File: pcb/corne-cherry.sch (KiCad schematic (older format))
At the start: 146 parts, among them J1 MJ-4PP-9, J2 OLED, J3 MJ-4PP-9, J4 OLED, J5 Conn_01x01_Male, J6 Conn_01x01_Male, P1 Conn_01x03, P3 Conn_01x03, SW1 SW_PUSH, SW10 SW_PUSH, SW11 SW_PUSH, SW12 SW_PUSH, SW13 SW_PUSH, SW14 SW_PUSH, SW15 SW_PUSH, SW16 SW_PUSH, SW17 SW_PUSH, SW18 SW_PUSH, SW19 SW_PUSH, SW2 SW_PUSH, SW20 SW_PUSH, SW21 SW_PUSH, SW22 SW_PUSH, SW23 SW_PUSH, SW24 SW_PUSH, SW25 SW_PUSH, SW26 SW_PUSH, SW27 SW_PUSH, SW28 SW_PUSH, SW29 SW_PUSH, SW3 SW_PUSH, SW30 SW_PUSH, SW31 SW_PUSH, SW32 SW_PUSH, SW33 SW_PUSH, SW34 SW_PUSH, SW35 SW_PUSH, SW36 SW_PUSH, SW37 SW_PUSH, SW38 SW_PUSH, SW39 SW_PUSH, SW4 SW_PUSH, SW40 SW_PUSH, SW41 SW_PUSH, SW42 SW_PUSH, SW43 Rotary_Encoder_Switch, SW44 Rotary_Encoder_Switch, SW5 SW_PUSH, SW6 SW_PUSH, SW7 SW_PUSH, SW8 SW_PUSH, SW9 SW_PUSH, U1 ProMicro, U2 ProMicro

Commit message: Add trackball support
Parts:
- added J7: Conn_01x05, other_parts:pimoroni_left_side_mount, symbol Connector_Generic:Conn_01x05
- J1, J3: symbol kbd:MJ-4PP-9 -> corne-cherry-rescue:MJ-4PP-9-kbd
- LED1, LED10, LED11, LED12, LED13, LED14, LED15, LED16, LED17, LED18, LED19, LED2, LED20, LED21, LED22, LED23, LED24, LED25, LED26, LED27, LED28, LED29, LED3, LED30, LED31, LED32, LED33, LED34, LED35, LED36, LED37, LED38, LED39, LED4, LED40, LED41, LED42, LED5, LED6, LED7, LED8, LED9: symbol kbd:YS-SK6812MINI-E -> corne-cherry-rescue:YS-SK6812MINI-E-kbd
- RSW1, RSW2, SW1, SW10, SW11, SW12, SW13, SW14, SW15, SW16, SW17, SW18, SW19, SW2, SW20, SW21, SW22, SW23, SW24, SW25, SW26, SW27, SW28, SW29, SW3, SW30, SW31, SW32, SW33, SW34, SW35, SW36, SW37, SW38, SW39, SW4, SW40, SW41, SW42, SW5, SW6, SW7, SW8, SW9: symbol kbd:SW_PUSH -> corne-cherry-rescue:SW_PUSH-kbd
- U1, U2: symbol kbd:ProMicro -> corne-cherry-rescue:ProMicro-kbd
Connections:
- wire segments 309 -> 313
- no-connect marks 8 -> 9

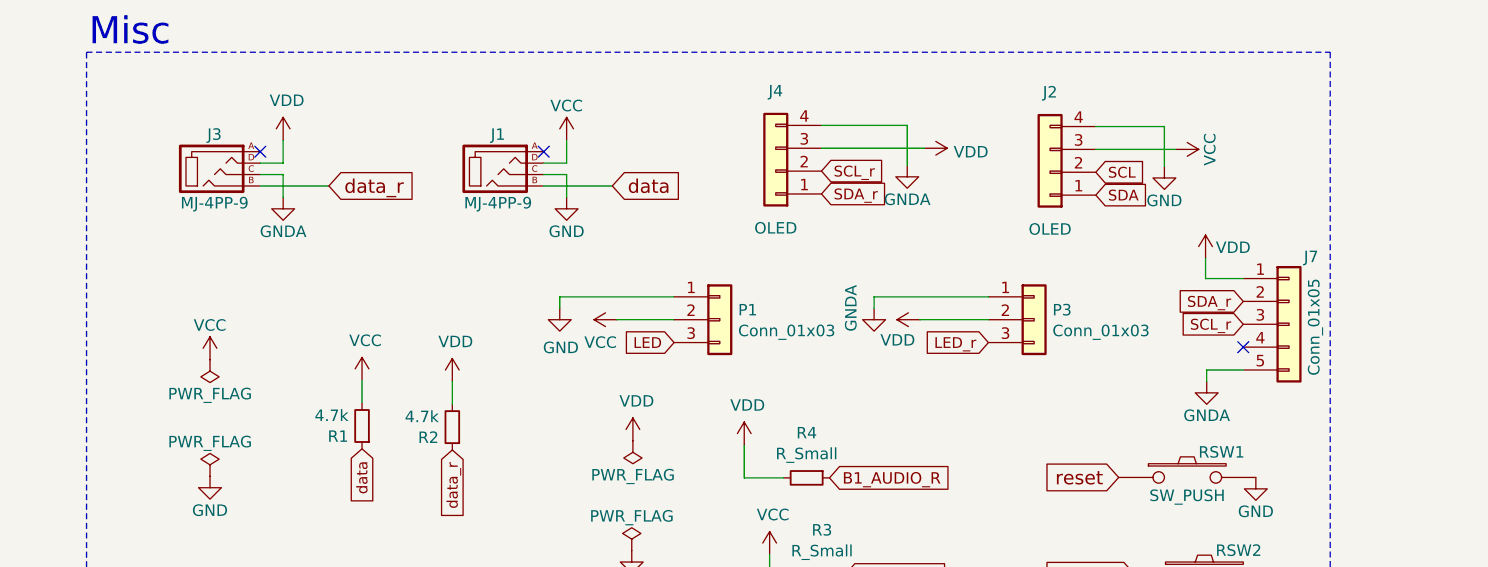
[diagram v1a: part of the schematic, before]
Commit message: Update markers and silkscreen
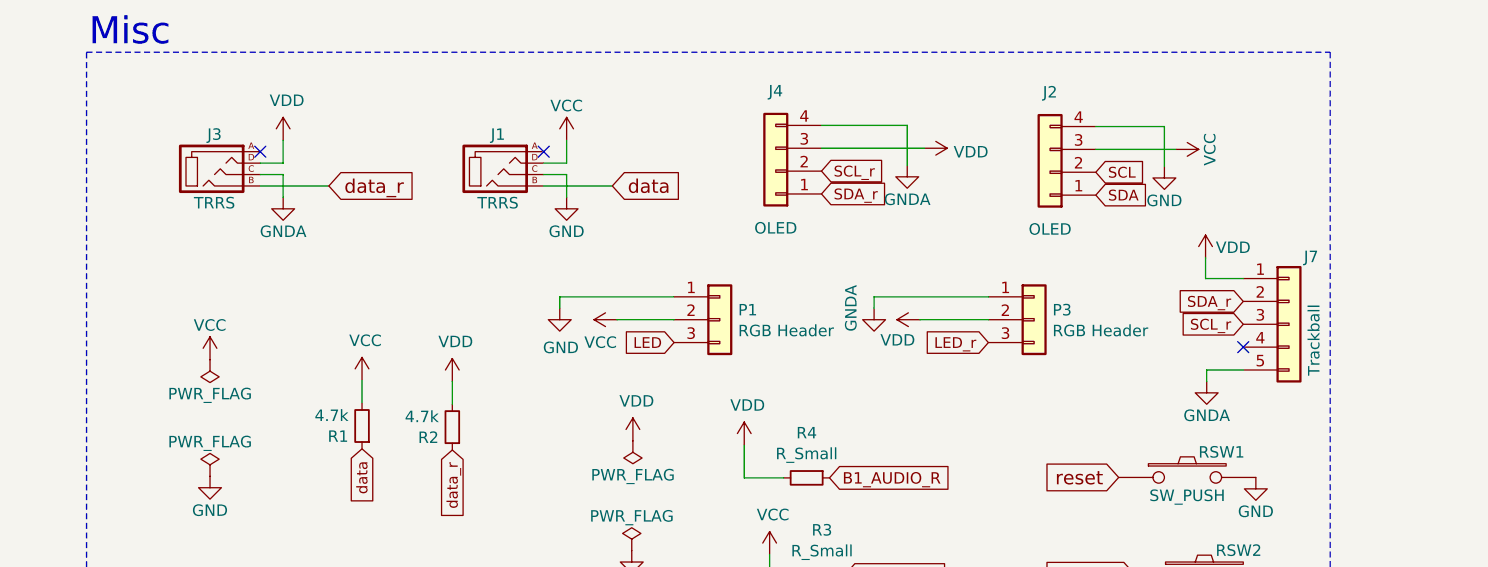
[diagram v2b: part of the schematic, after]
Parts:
- J1, J3: value MJ-4PP-9 -> TRRS
- J7: value Conn_01x05 -> Trackball
- P1, P3: value Conn_01x03 -> RGB Header
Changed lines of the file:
@@
 P 3910 1325
 F 0 "J1" H 3910 1475 50  0000 C CNN
-F 1 "MJ-4PP-9" H 3910 1175 50  0000 C CNN
+F 1 "TRRS" H 3910 1175 50  0000 C CNN
 F 2 "kbd:MJ-4PP-9_1side" H 4185 1500 50  0001 C CNN
 F 3 "" H 4185 1500 50  0001 C CNN
@@
 P 2670 1325
 F 0 "J3" H 2670 1475 50  0000 C CNN
-F 1 "MJ-4PP-9" H 2670 1175 50  0000 C CNN
+F 1 "TRRS" H 2670 1175 50  0000 C CNN
 F 2 "kbd:MJ-4PP-9_1side" H 2945 1500 50  0001 C CNN
 F 3 "" H 2945 1500 50  0001 C CNN
@@
 P 6255 1985
 F 0 "P3" H 6335 2027 50  0000 L CNN
-F 1 "Conn_01x03" H 6335 1936 50  0000 L CNN
+F 1 "RGB Header" H 6335 1936 50  0000 L CNN
 F 2 "Connector_PinSocket_2.54mm:PinSocket_1x03_P2.54mm_Horizontal" H 6255 1985 50  0001 C CNN
 F 3 "~" H 6255 1985 50  0001 C CNN
@@
 P 4880 1985
 F 0 "P1" H 4960 2027 50  0000 L CNN
-F 1 "Conn_01x03" H 4960 1936 50  0000 L CNN
+F 1 "RGB Header" H 4960 1936 50  0000 L CNN
 F 2 "Connector_PinSocket_2.54mm:PinSocket_1x03_P2.54mm_Vertical" H 4880 1985 50  0001 C CNN
 F 3 "~" H 4880 1985 50  0001 C CNN
@@
 P 7370 2005
 F 0 "J7" H 7435 2300 50  0000 L CNN
-F 1 "Conn_01x05" V 7480 1780 50  0000 L CNN
+F 1 "Trackball" V 7480 1780 50  0000 L CNN
 F 2 "other_parts:pimoroni_left_side_mount" H 7370 2005 50  0001 C CNN
 F 3 "~" H 7370 2005 50  0001 C CNN

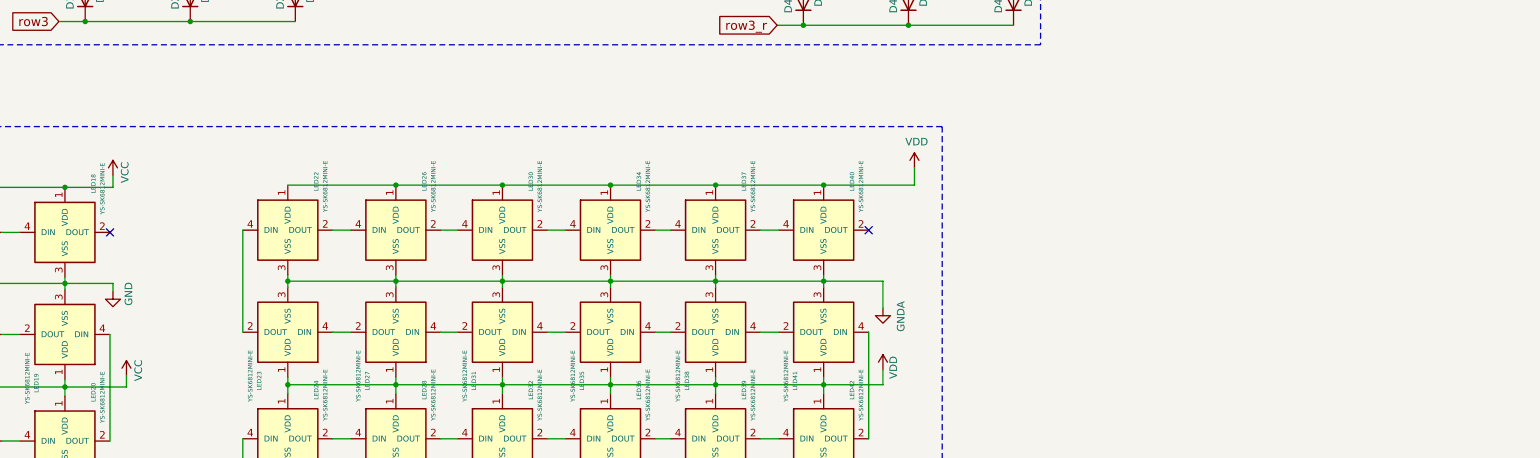
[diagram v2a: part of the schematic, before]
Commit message: some underglow stuff on left half
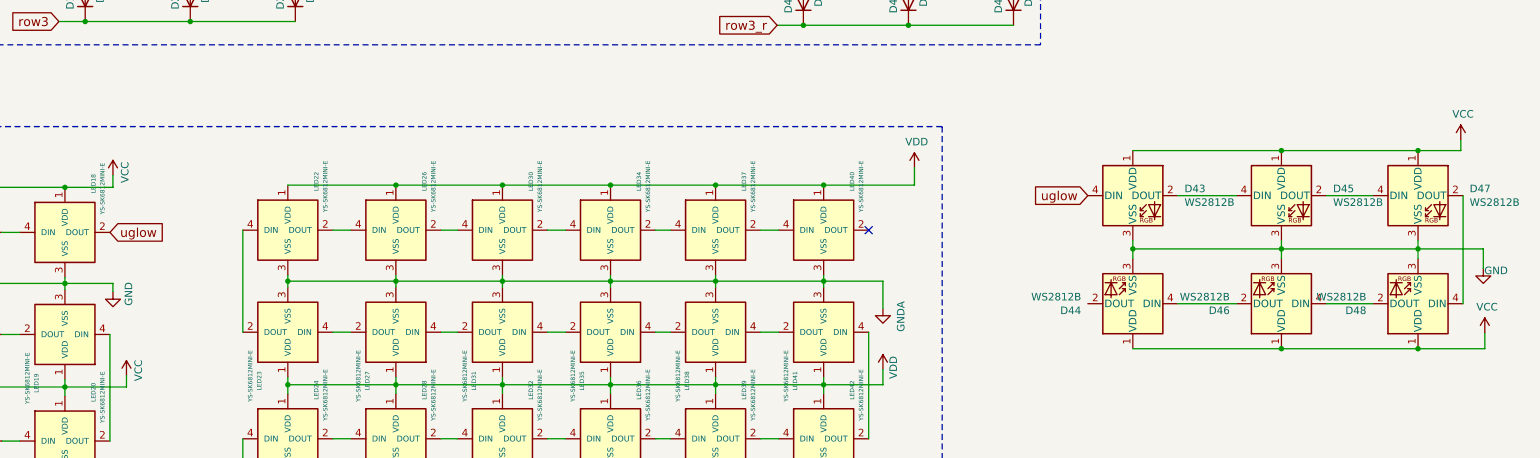
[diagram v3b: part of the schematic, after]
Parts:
- added D43, D44, D45, D46, D47, D48: WS2812B, Keebio-Parts:WS2812B, symbol LED:WS2812B
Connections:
- net GND: now also D43.3 (VSS), D44.3 (VSS), D45.3 (VSS), D46.3 (VSS), D47.3 (VSS), D48.3 (VSS)
- net VCC: now also D43.1 (VDD), D44.1 (VDD), D45.1 (VDD), D46.1 (VDD), D47.1 (VDD), D48.1 (VDD)
- net uglow: now reaches LED18.2 (DOUT)
- net uglow: now also D43.4 (DIN)
- new net: D43.2 (DOUT), D45.4 (DIN)
- new net: D45.2 (DOUT), D47.4 (DIN)
- new net: D47.2 (DOUT), D48.4 (DIN)
- new net: D46.4 (DIN), D48.2 (DOUT)
- new net: D44.4 (DIN), D46.2 (DOUT)
- no-connect marks 9 -> 8
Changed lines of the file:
@@
 Wire Wire Line
 	1420 8990 1300 8990
-NoConn ~ 4870 8310
 Wire Wire Line
 	1000 8650 1720 8650
@@
 Text GLabel 7170 2005 0    47   Input ~ 0
 SCL_r
+$Comp
+L LED:WS2812B D43
+U 1 1 60D8D511
+P 11685 8065
+F 0 "D43" H 12029 8111 50  0000 L CNN
+F 1 "WS2812B" H 12029 8020 50  0000 L CNN
+F 2 "Keebio-Parts:WS2812B" H 11735 7765 50  0001 L TNN
+F 3 "https://cdn-shop.adafruit.com/datasheets/WS2812B.pdf" H 11785 7690 50  0001 L TNN
+	1    11685 8065
+	1    0    0    -1
+$EndComp
+$Comp
+L LED:WS2812B D45
+U 1 1 60D8F5FE
+P 12675 8065
+F 0 "D45" H 13019 8111 50  0000 L CNN
+F 1 "WS2812B" H 13019 8020 50  0000 L CNN
+F 2 "Keebio-Parts:WS2812B" H 12725 7765 50  0001 L TNN
+F 3 "https://cdn-shop.adafruit.com/datasheets/WS2812B.pdf" H 12775 7690 50  0001 L TNN
+	1    12675 8065
+	1    0    0    -1
+$EndComp
+Wire Wire Line
+	11985 8065 12375 8065
+$Comp
+L LED:WS2812B D47
+U 1 1 60DAA5B2
+P 13585 8065
+F 0 "D47" H 13929 8111 50  0000 L CNN
+F 1 "WS2812B" H 13929 8020 50  0000 L CNN
+F 2 "Keebio-Parts:WS2812B" H 13635 7765 50  0001 L TNN
+F 3 "https://cdn-shop.adafruit.com/datasheets/WS2812B.pdf" H 13685 7690 50  0001 L TNN
+	1    13585 8065
+	1    0    0    -1
+$EndComp
+Wire Wire Line
+	12975 8065 13285 8065
+$Comp
+L LED:WS2812B D48
+U 1 1 60DC8763
+P 13585 8785
+F 0 "D48" H 13929 8831 50  0000 L CNN
+F 1 "WS2812B" H 13929 8740 50  0000 L CNN
+F 2 "Keebio-Parts:WS2812B" H 13635 8485 50  0001 L TNN
+F 3 "https://cdn-shop.adafruit.com/datasheets/WS2812B.pdf" H 13685 8410 50  0001 L TNN
+	1    13585 8785
+	-1   0    0    1
+$EndComp
+$Comp
+L LED:WS2812B D46
+U 1 1 60DC8CAF
+P 12675 8785
+F 0 "D46" H 13019 8831 50  0000 L CNN
+F 1 "WS2812B" H 13019 8740 50  0000 L CNN
+F 2 "Keebio-Parts:WS2812B" H 12725 8485 50  0001 L TNN
+F 3 "https://cdn-shop.adafruit.com/datasheets/WS2812B.pdf" H 12775 8410 50  0001 L TNN
+	1    12675 8785
+	-1   0    0    1
+$EndComp
+Wire Wire Line
+	11985 8785 12375 8785
+$Comp
+L LED:WS2812B D44
+U 1 1 60DC8CBA
+P 11685 8785
+F 0 "D44" H 12029 8831 50  0000 L CNN
+F 1 "WS2812B" H 12029 8740 50  0000 L CNN
+F 2 "Keebio-Parts:WS2812B" H 11735 8485 50  0001 L TNN
+F 3 "https://cdn-shop.adafruit.com/datasheets/WS2812B.pdf" H 11785 8410 50  0001 L TNN
+	1    11685 8785
+	-1   0    0    1
+$EndComp
+Wire Wire Line
+	12975 8785 13285 8785
+Text GLabel 4870 8310 2    60   Input ~ 0
+uglow
+Text GLabel 11385 8065 0    60   Input ~ 0
+uglow
+Wire Wire Line
+	13885 8065 13885 8785
+Wire Wire Line
+	11685 8485 11685 8420
+Wire Wire Line
+	11685 8420 12675 8420
+Wire Wire Line
+	14020 8420 14020 8550
+Wire Wire Line
+	11685 8365 11685 8420
+Connection ~ 11685 8420
+Wire Wire Line
+	12675 8485 12675 8420
+Connection ~ 12675 8420
+Wire Wire Line
+	12675 8420 13585 8420
+Wire Wire Line
+	12675 8365 12675 8420
+Wire Wire Line
+	13585 8485 13585 8420
+Connection ~ 13585 8420
+Wire Wire Line
+	13585 8420 14020 8420
+Wire Wire Line
+	13585 8365 13585 8420
+$Comp
+L power:GND #PWR0123
+U 1 1 60F413B7
+P 14020 8550
+F 0 "#PWR0123" H 14020 8300 50  0001 C CNN
+F 1 "GND" H 14105 8535 50  0000 C CNN
+F 2 "" H 14020 8550 50  0001 C CNN
+F 3 "" H 14020 8550 50  0001 C CNN
+	1    14020 8550
+	1    0    0    -1
+$EndComp
+Wire Wire Line
+	11685 7765 12675 7765
+Wire Wire Line
+	13870 7765 13870 7695
+Connection ~ 12675 7765
+Wire Wire Line
+	12675 7765 13585 7765
+Connection ~ 13585 7765
+Wire Wire Line
+	13585 7765 13870 7765
+$Comp
+L power:VCC #PWR0124
+U 1 1 60FEAFF3
+P 13870 7695
+F 0 "#PWR0124" H 13870 7545 50  0001 C CNN
+F 1 "VCC" H 13885 7868 50  0000 C CNN
+F 2 "" H 13870 7695 50  0001 C CNN
+F 3 "" H 13870 7695 50  0001 C CNN
+	1    13870 7695
+	1    0    0    -1
+$EndComp
+Wire Wire Line
+	11685 9085 12675 9085
+Wire Wire Line
+	14030 9085 14030 8980
+Connection ~ 12675 9085
+Wire Wire Line
+	12675 9085 13585 9085
+Connection ~ 13585 9085
+Wire Wire Line
+	13585 9085 14030 9085
+$Comp
+L power:VCC #PWR0125
+U 1 1 6100B6CC
+P 14030 8980
+F 0 "#PWR0125" H 14030 8830 50  0001 C CNN
+F 1 "VCC" H 14045 9153 50  0000 C CNN
+F 2 "" H 14030 8980 50  0001 C CNN
+F 3 "" H 14030 8980 50  0001 C CNN
+	1    14030 8980
+	1    0    0    -1
+$EndComp
 $EndSCHEMATC

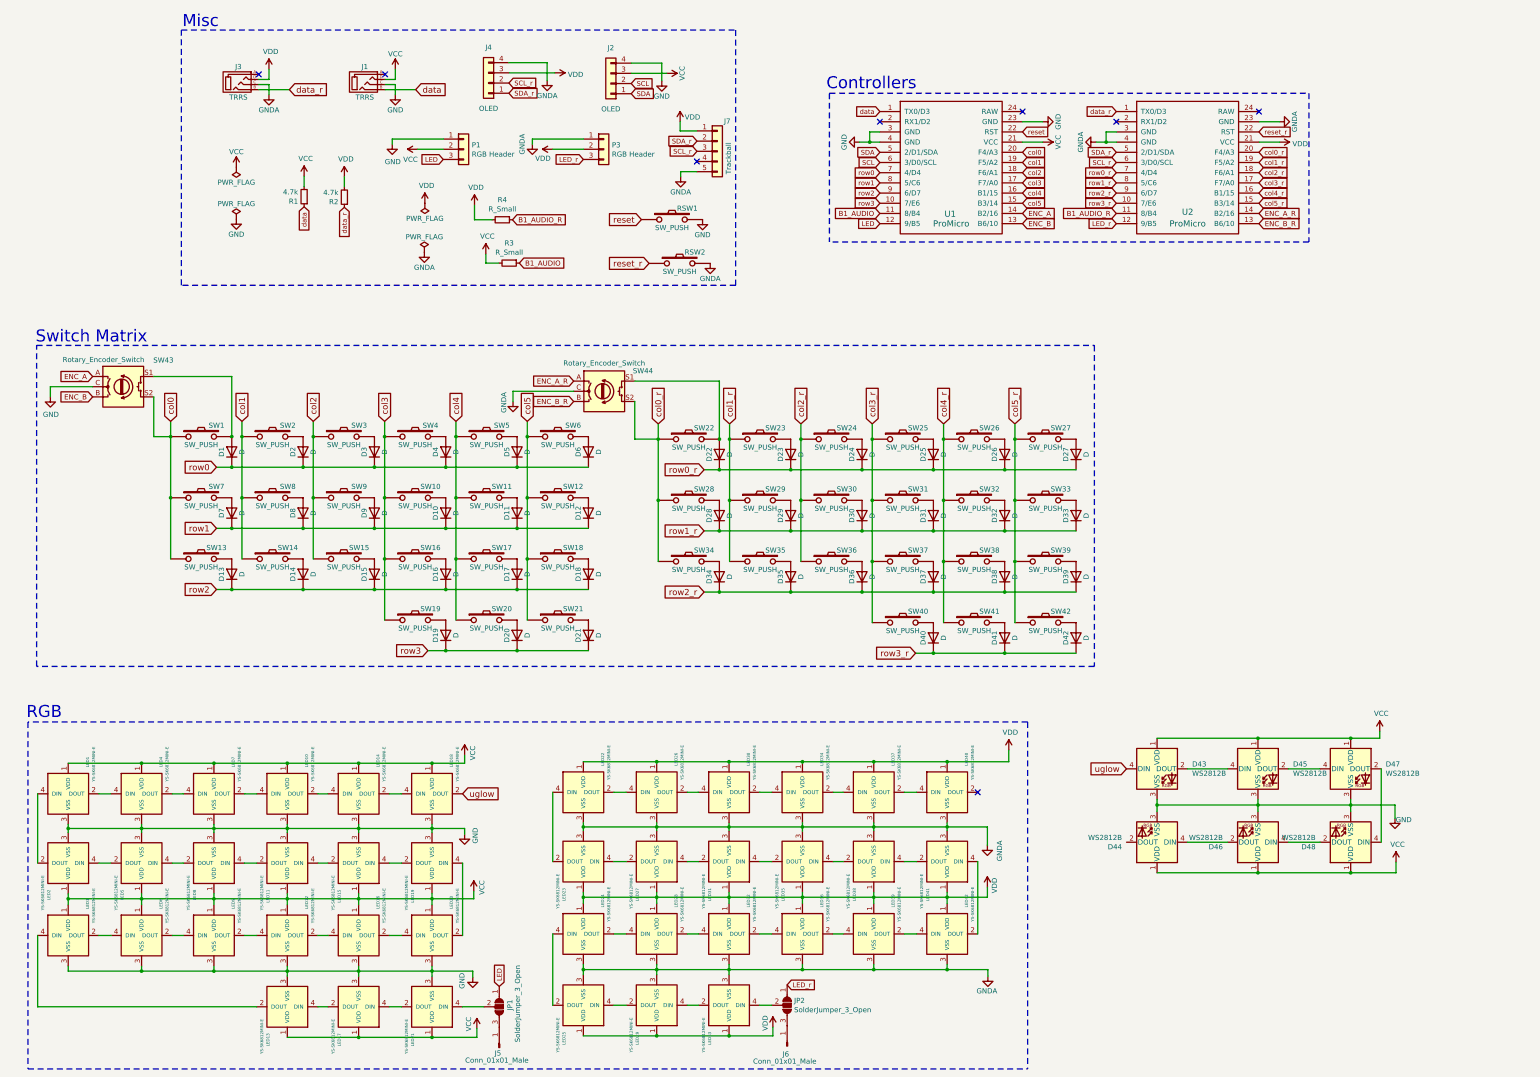
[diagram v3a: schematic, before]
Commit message: Finish underglow and add SMD resistor foorprints
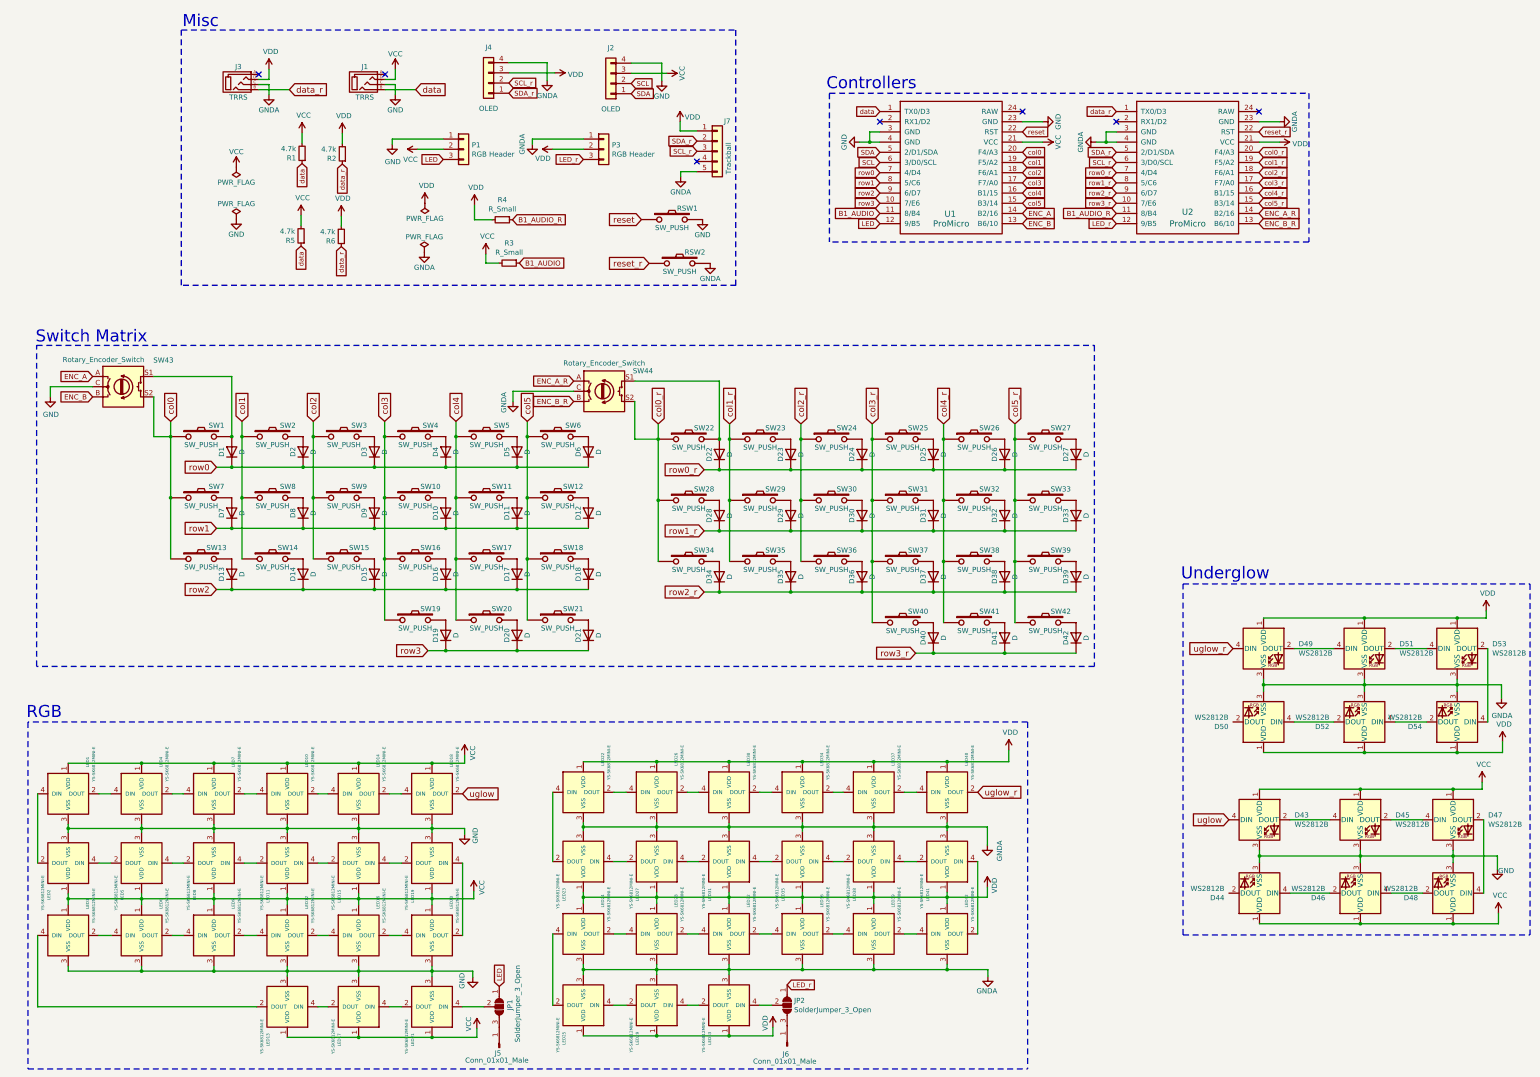
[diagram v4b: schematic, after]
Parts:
- added D49, D50, D51, D52, D53, D54: WS2812B, Keebio-Parts:WS2812B, symbol LED:WS2812B
- added R5, R6: 4.7k, Keebio-Parts:R_0805, symbol Device:R_Small
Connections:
- net GNDA: now also D49.3 (VSS), D50.3 (VSS), D51.3 (VSS), D52.3 (VSS), D53.3 (VSS), D54.3 (VSS)
- net VCC: now also R5.2
- net VDD: now also D49.1 (VDD), D50.1 (VDD), D51.1 (VDD), D52.1 (VDD), D53.1 (VDD), D54.1 (VDD), R6.2
- net data: now also R5.1
- net data_r: now also R6.1
- net uglow_r: now reaches LED40.2 (DOUT)
- net uglow_r: now also D49.4 (DIN)
- new net: D50.4 (DIN), D52.2 (DOUT)
- new net: D52.4 (DIN), D54.2 (DOUT)
- new net: D53.2 (DOUT), D54.4 (DIN)
- new net: D51.2 (DOUT), D53.4 (DIN)
- new net: D49.2 (DOUT), D51.4 (DIN)
- no-connect marks 8 -> 7
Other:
- note added: "Underglow\n"
- moved on the sheet: D43, D44, D45, D46, D47, D48, R1, R2

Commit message: Fix RGB positions
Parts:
- D1, D10, D11, D12, D13, D14, D15, D16, D17, D18, D19, D2, D20, D21, D22, D23, D24, D25, D26, D27, D28, D29, D3, D30, D31, D32, D33, D34, D35, D36, D37, D38, D39, D4, D40, D41, D42, D5, D6, D7, D8, D9: symbol Device:D -> corne-cherry-rescue:D-Device
- D43, D44, D45, D46, D47, D48, D49, D50, D51, D52, D53, D54: symbol LED:WS2812B -> corne-cherry-rescue:WS2812B-LED
- J2, J4: symbol Connector_Generic:Conn_01x04 -> corne-cherry-rescue:Conn_01x04-Connector_Generic
- J5, J6: symbol Connector:Conn_01x01_Male -> corne-cherry-rescue:Conn_01x01_Male-Connector
- J7: symbol Connector_Generic:Conn_01x05 -> corne-cherry-rescue:Conn_01x05-Connector_Generic
- JP1, JP2: symbol Jumper:SolderJumper_3_Open -> corne-cherry-rescue:SolderJumper_3_Open-Jumper
- P1, P3: symbol Connector_Generic:Conn_01x03 -> corne-cherry-rescue:Conn_01x03-Connector_Generic
- R1, R2, R3, R4, R5, R6: symbol Device:R_Small -> corne-cherry-rescue:R_Small-Device
- SW43, SW44: symbol Device:Rotary_Encoder_Switch -> corne-cherry-rescue:Rotary_Encoder_Switch-Device
